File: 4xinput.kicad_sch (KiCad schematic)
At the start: 6 parts, among them J3 In1, J4 In2, J5 In3, J6 In4, U17 HEF4021BT

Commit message: Get board name and version from text variable
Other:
- title: (none) -> ${BoardName}
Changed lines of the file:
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@@
 	(generator_version "8.99")
 	(paper "A4")
+	(title_block
+		(title "${BoardName}")
+		(date "2024-11-11")
+		(rev "${Version}")
+	)
 	(junction
 		(at 85.09 71.12)

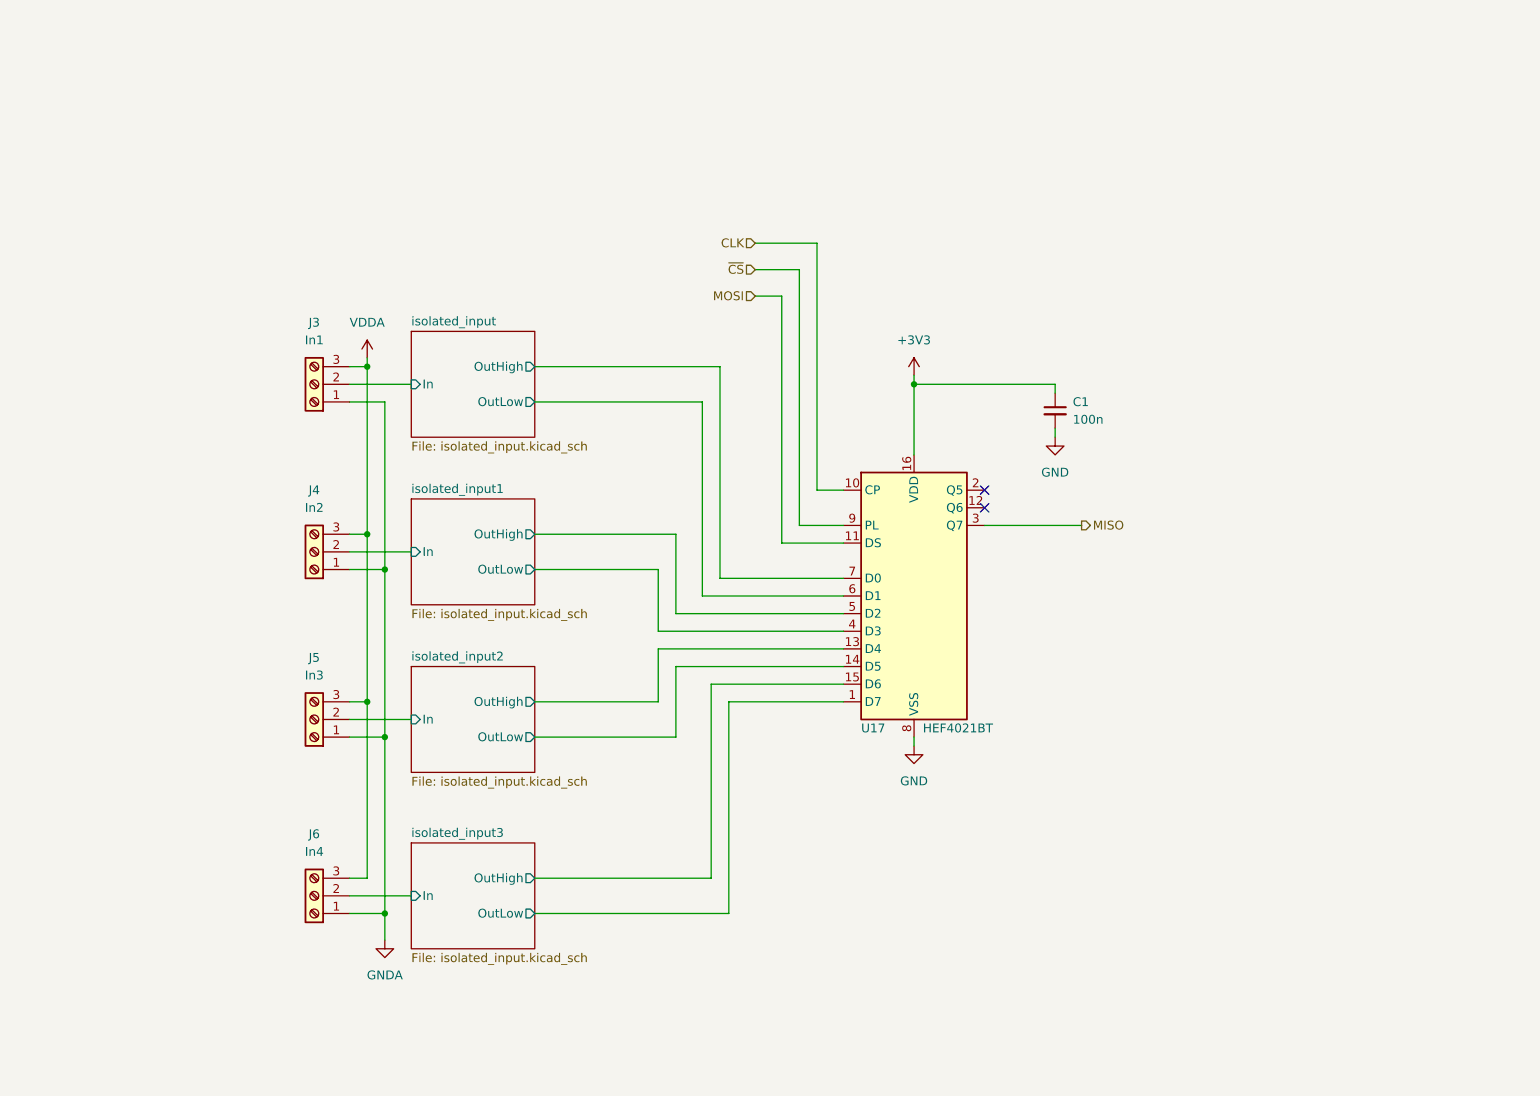
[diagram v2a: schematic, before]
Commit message: Change optocouplers, improve power routing
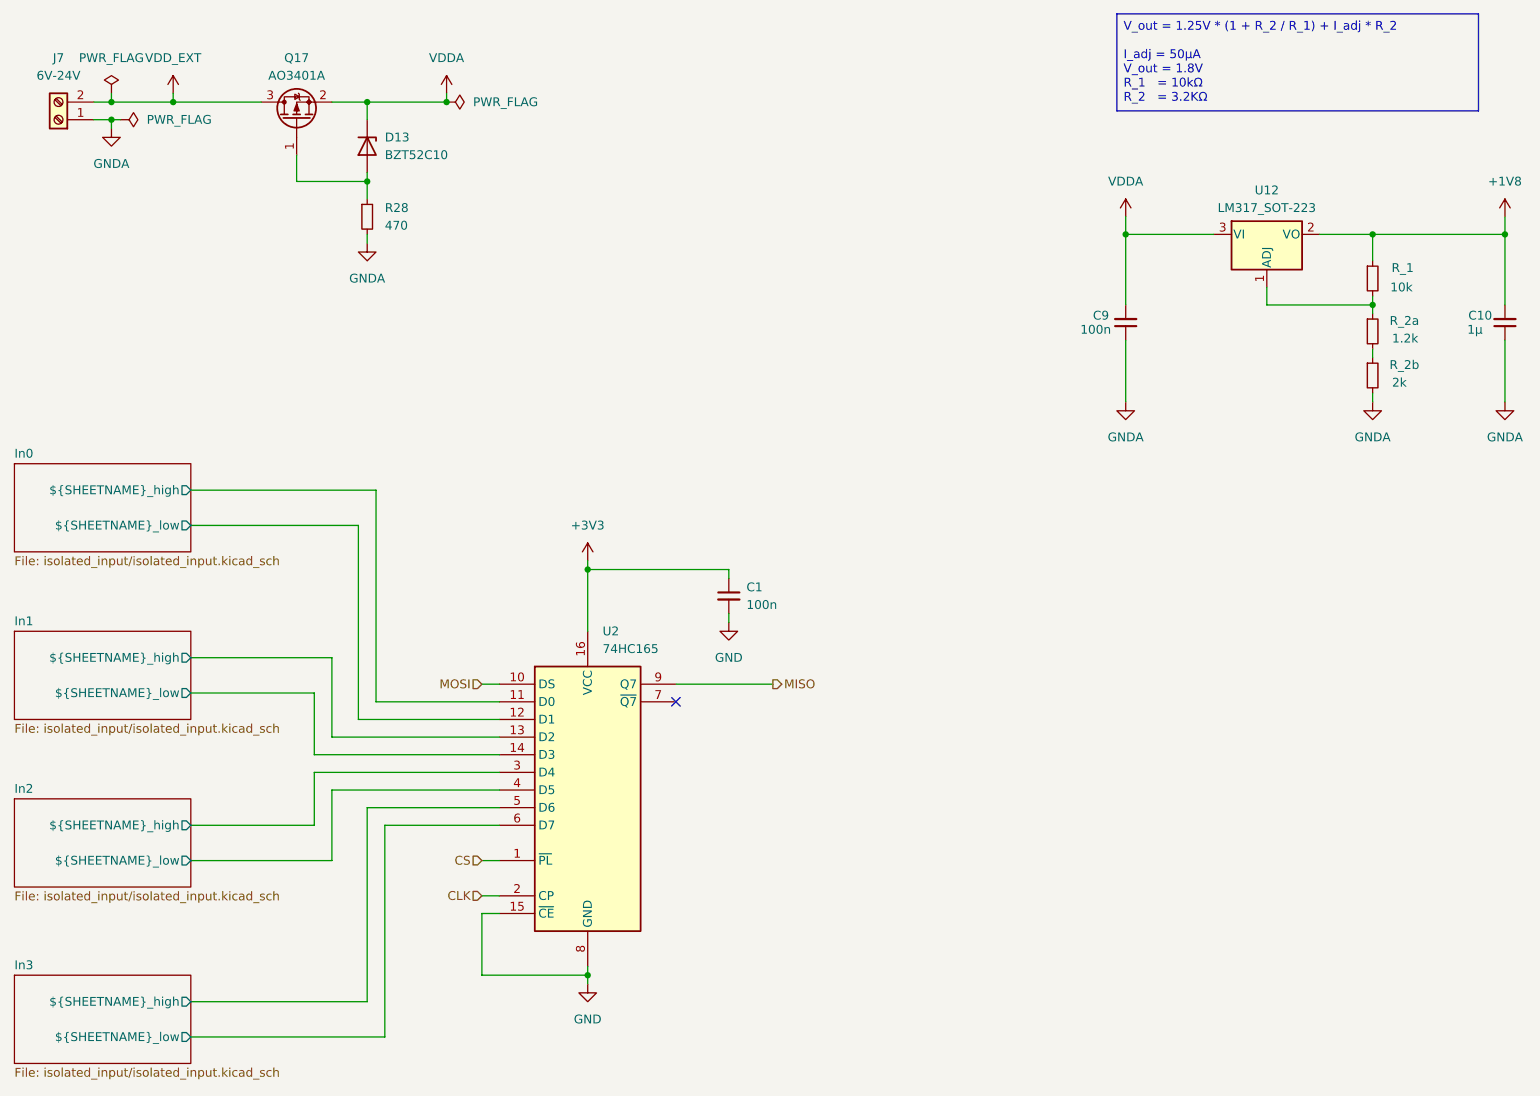
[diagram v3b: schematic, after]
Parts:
- removed J3: In1, Connector_Molex:Molex_KK-254_AE-6410-03A_1x03_P2.54mm_Vertical, symbol Connector:Screw_Terminal_01x03
- removed J4: In2, Connector_Molex:Molex_KK-254_AE-6410-03A_1x03_P2.54mm_Vertical, symbol Connector:Screw_Terminal_01x03
- removed J5: In3, Connector_Molex:Molex_KK-254_AE-6410-03A_1x03_P2.54mm_Vertical, symbol Connector:Screw_Terminal_01x03
- removed J6: In4, Connector_Molex:Molex_KK-254_AE-6410-03A_1x03_P2.54mm_Vertical, symbol Connector:Screw_Terminal_01x03
- removed U17: HEF4021BT, Package_SO:SOIC-16_4.55x10.3mm_P1.27mm, symbol 4xxx:4021
- added C10: 1µ, Capacitor_SMD:C_0603_1608Metric, symbol Device:C_Small
- added C9: 100n, Capacitor_SMD:C_0603_1608Metric, symbol Device:C_Small
- added D13: BZT52C10, Diode_SMD:D_SOD-123, symbol Device:D_Zener
- added J7: 6V-24V, lcsc_stuff:KF141V-2.54-2P, symbol Connector:Screw_Terminal_01x02
- added Q17: AO3401A, Package_TO_SOT_SMD:SOT-23, symbol Transistor_FET:AO3401A
- added R26: 10k, Resistor_SMD:R_0603_1608Metric, symbol Device:R_Small
- added R27: 1.2k, Resistor_SMD:R_0603_1608Metric, symbol Device:R_Small
- added R28: 470, Resistor_SMD:R_0402_1005Metric_Pad0.72x0.64mm_HandSolder, symbol Device:R_Small
- added R29: 2k, Resistor_SMD:R_0603_1608Metric, symbol Device:R_Small
- added U12: LM317_SOT-223, Package_TO_SOT_SMD:SOT-223-3_TabPin2, symbol Regulator_Linear:LM317_SOT-223
- added U2: 74HC165, Package_SO:SO-16_3.9x9.9mm_P1.27mm, symbol 74xx:74HC165
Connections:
- net +3V3: now also U2.16 (VCC)
- net CLK: now also U2.2 (CP)
- net GND: now also U2.15 (~{CE}), U2.8 (GND)
- net GNDA: now also C10.1, C9.1, J7.1 (Pin_1), R28.2, R29.2
- net MISO: now also U2.9 (Q7)
- net MOSI: now also U2.10 (DS)
- net VDDA: now also C9.2, D13.1 (K), Q17.2 (S), U12.3 (VI)
- new net: D13.2 (A), Q17.1 (G), R28.1
- new net: R27.2, R29.1
- new net: R26.2, R27.1, U12.1 (ADJ)
- new net +1V8: C10.2, R26.1, U12.2 (VO)
- new net CS: U2.1 (~{PL})
- new net In0/${SHEETNAME}_high: U2.11 (D0)
- new net In0/${SHEETNAME}_low: U2.12 (D1)
- new net In1/${SHEETNAME}_high: U2.13 (D2)
- new net In1/${SHEETNAME}_low: U2.14 (D3)
- new net In2/${SHEETNAME}_high: U2.3 (D4)
- new net In2/${SHEETNAME}_low: U2.4 (D5)
- new net In3/${SHEETNAME}_high: U2.5 (D6)
- new net In3/${SHEETNAME}_low: U2.6 (D7)
- new net VDD_EXT: J7.2 (Pin_2), Q17.3 (D)
- no-connect marks 2 -> 1
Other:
- removed sheet isolated_input
- removed sheet isolated_input1
- removed sheet isolated_input2
- removed sheet isolated_input3
- added sheet In0 (isolated_input/isolated_input.kicad_sch)
- added sheet In1 (isolated_input/isolated_input.kicad_sch)
- added sheet In2 (isolated_input/isolated_input.kicad_sch)
- added sheet In3 (isolated_input/isolated_input.kicad_sch)
- moved on the sheet: C1
